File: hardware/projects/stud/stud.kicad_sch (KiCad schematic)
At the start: 89 parts, among them IC1 R7KA8M2JFLCAC#UC0, IC2 IS42S32160F-7BLI, J1 USB_C_Receptacle_USB2.0_16P, J10 SCL1_A, J11 SDA1_A, J2 DAC0, J3 ADC1_8, J4 DAC1, J5 ADC1_6, J6 ADC1_0, J7 ADC1_2, J8 SCL0_A, J9 SDA0_A, U1 TPS629210DRLR, U2 TAC5242, Y1 X1G0044510004

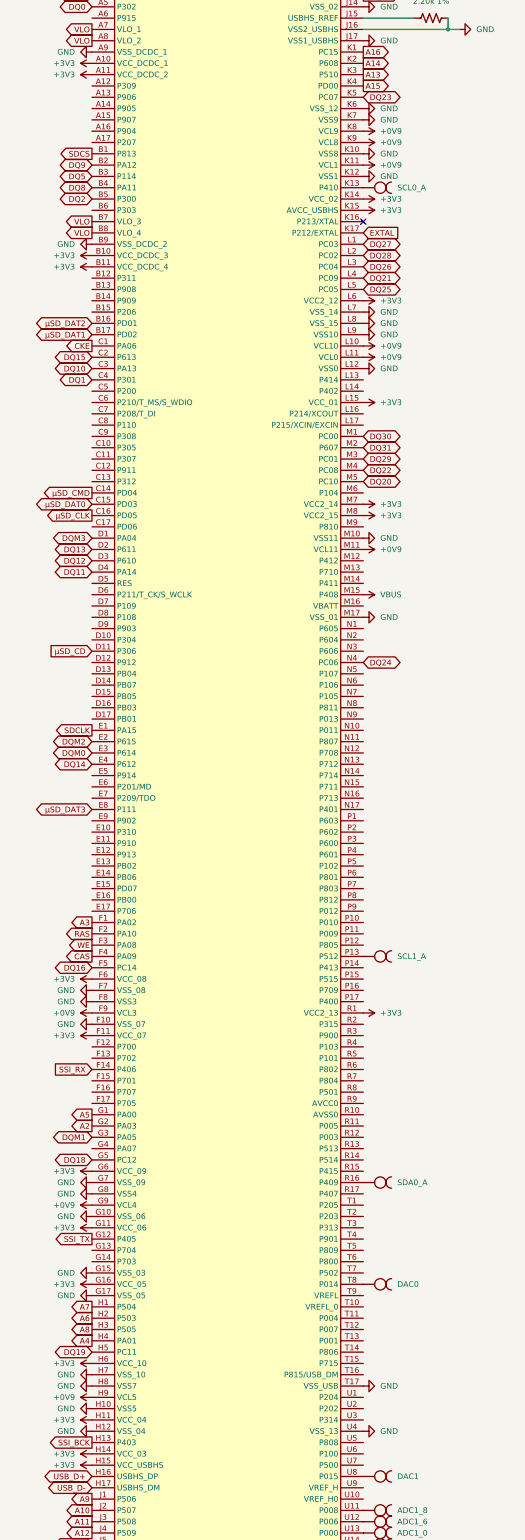
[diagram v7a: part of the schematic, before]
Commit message: claude: draft GPIO connections
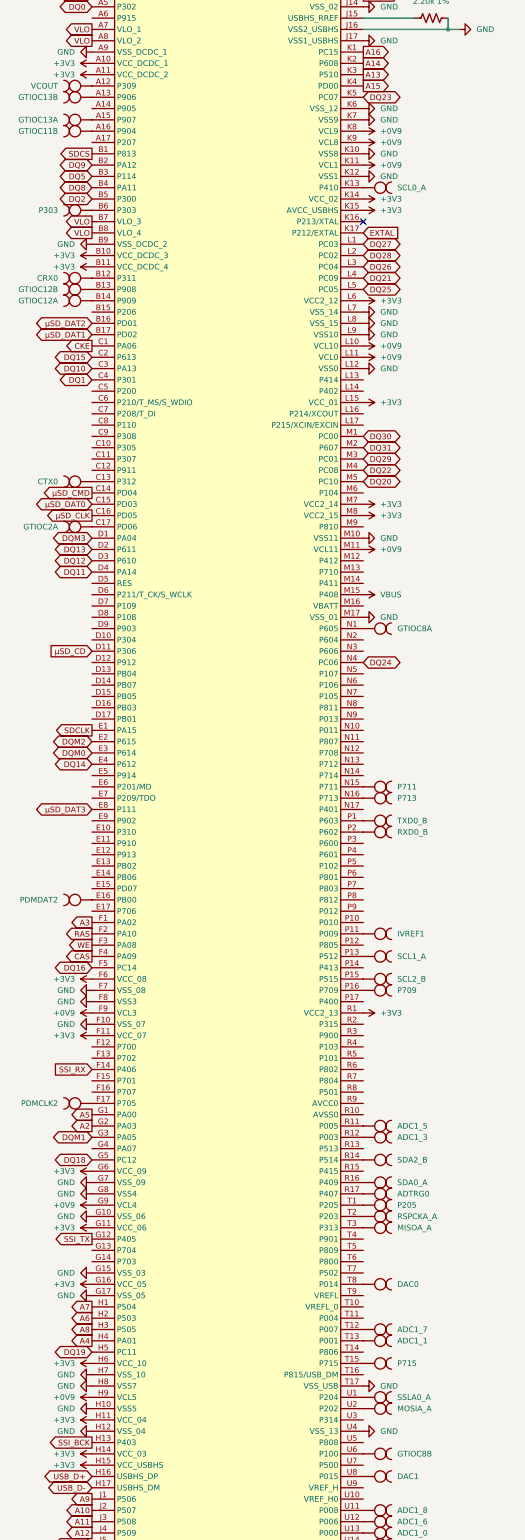
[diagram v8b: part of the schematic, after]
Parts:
- added J12: SCL2_B, custom:Connector_01x01_CastellatedEdge, symbol custom:Connector_01x01_CastellatedEdge
- added J13: SDA2_B, custom:Connector_01x01_CastellatedEdge, symbol custom:Connector_01x01_CastellatedEdge
- added J14: RSPCKA_A, custom:Connector_01x01_CastellatedEdge, symbol custom:Connector_01x01_CastellatedEdge
- added J15: MOSIA_A, custom:Connector_01x01_CastellatedEdge, symbol custom:Connector_01x01_CastellatedEdge
- added J16: MISOA_A, custom:Connector_01x01_CastellatedEdge, symbol custom:Connector_01x01_CastellatedEdge
- added J17: SSLA0_A, custom:Connector_01x01_CastellatedEdge, symbol custom:Connector_01x01_CastellatedEdge
- added J18: CTX0, custom:Connector_01x01_CastellatedEdge, symbol custom:Connector_01x01_CastellatedEdge
- added J19: CRX0, custom:Connector_01x01_CastellatedEdge, symbol custom:Connector_01x01_CastellatedEdge
- added J20: GTIOC13A, custom:Connector_01x01_CastellatedEdge, symbol custom:Connector_01x01_CastellatedEdge
- added J21: GTIOC13B, custom:Connector_01x01_CastellatedEdge, symbol custom:Connector_01x01_CastellatedEdge
- added J22: GTIOC12A, custom:Connector_01x01_CastellatedEdge, symbol custom:Connector_01x01_CastellatedEdge
- added J23: GTIOC12B, custom:Connector_01x01_CastellatedEdge, symbol custom:Connector_01x01_CastellatedEdge
- added J24: GTIOC11B, custom:Connector_01x01_CastellatedEdge, symbol custom:Connector_01x01_CastellatedEdge
- added J25: GTIOC2A, custom:Connector_01x01_CastellatedEdge, symbol custom:Connector_01x01_CastellatedEdge
- added J26: GTIOC8A, custom:Connector_01x01_CastellatedEdge, symbol custom:Connector_01x01_CastellatedEdge
- added J27: GTIOC8B, custom:Connector_01x01_CastellatedEdge, symbol custom:Connector_01x01_CastellatedEdge
- added J28: TXD0_B, custom:Connector_01x01_CastellatedEdge, symbol custom:Connector_01x01_CastellatedEdge
- added J29: RXD0_B, custom:Connector_01x01_CastellatedEdge, symbol custom:Connector_01x01_CastellatedEdge
- added J30: VCOUT, custom:Connector_01x01_CastellatedEdge, symbol custom:Connector_01x01_CastellatedEdge
- added J31: IVREF1, custom:Connector_01x01_CastellatedEdge, symbol custom:Connector_01x01_CastellatedEdge
- added J32: ADC1_1, custom:Connector_01x01_CastellatedEdge, symbol custom:Connector_01x01_CastellatedEdge
- added J33: ADC1_3, custom:Connector_01x01_CastellatedEdge, symbol custom:Connector_01x01_CastellatedEdge
- added J34: ADC1_5, custom:Connector_01x01_CastellatedEdge, symbol custom:Connector_01x01_CastellatedEdge
- added J35: ADC1_7, custom:Connector_01x01_CastellatedEdge, symbol custom:Connector_01x01_CastellatedEdge
- added J36: ADTRG0, custom:Connector_01x01_CastellatedEdge, symbol custom:Connector_01x01_CastellatedEdge
- added J37: PDMCLK2, custom:Connector_01x01_CastellatedEdge, symbol custom:Connector_01x01_CastellatedEdge
- added J38: PDMDAT2, custom:Connector_01x01_CastellatedEdge, symbol custom:Connector_01x01_CastellatedEdge
- added J39: P205, custom:Connector_01x01_CastellatedEdge, symbol custom:Connector_01x01_CastellatedEdge
- added J40: P303, custom:Connector_01x01_CastellatedEdge, symbol custom:Connector_01x01_CastellatedEdge
- added J41: P709, custom:Connector_01x01_CastellatedEdge, symbol custom:Connector_01x01_CastellatedEdge
- added J42: P711, custom:Connector_01x01_CastellatedEdge, symbol custom:Connector_01x01_CastellatedEdge
- added J43: P713, custom:Connector_01x01_CastellatedEdge, symbol custom:Connector_01x01_CastellatedEdge
- added J44: P715, custom:Connector_01x01_CastellatedEdge, symbol custom:Connector_01x01_CastellatedEdge
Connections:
- net at IC1.A12 (P309): now also J30.1
- net at IC1.A13 (P906): now also J21.1
- net at IC1.A15 (P907): now also J20.1
- net at IC1.A16 (P904): now also J24.1
- net at IC1.B12 (P311): now also J19.1
- net at IC1.B13 (P908): now also J23.1
- net at IC1.B14 (P909): now also J22.1
- net at IC1.B6 (P303): now also J40.1
- net at IC1.C13 (P312): now also J18.1
- net at IC1.C17 (PD06): now also J25.1
- net at IC1.E16 (PB00): now also J38.1
- net at IC1.F17 (P705): now also J37.1
- net at IC1.N1 (P605): now also J26.1
- net at IC1.N15 (P711): now also J42.1
- net at IC1.N16 (P713): now also J43.1
- net at IC1.P1 (P603): now also J28.1
- net at IC1.P11 (P009): now also J31.1
- net at IC1.P15 (P515): now also J12.1
- net at IC1.P16 (P709): now also J41.1
- net at IC1.P2 (P602): now also J29.1
- net at IC1.R11 (P005): now also J34.1
- net at IC1.R12 (P003): now also J33.1
- net at IC1.R14 (P514): now also J13.1
- net at IC1.R17 (P407): now also J36.1
- net at IC1.T1 (P205): now also J39.1
- net at IC1.T12 (P007): now also J35.1
- net at IC1.T13 (P001): now also J32.1
- net at IC1.T15 (P715): now also J44.1
- net at IC1.T2 (P203): now also J14.1
- net at IC1.T3 (P313): now also J16.1
- net at IC1.U1 (P204): now also J17.1
- net at IC1.U2 (P202): now also J15.1
- net at IC1.U6 (P100): now also J27.1
